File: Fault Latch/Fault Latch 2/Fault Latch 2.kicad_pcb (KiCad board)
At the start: 2 copper layers, 110 x 90 mm, 108 parts, among them K101 Fujitsu_FTR-LYAA005x, K102 Fujitsu_FTR-LYAA005x, K103 Fujitsu_FTR-LYAA005x, Q101 Q_NPN_BEC, Q102 Q_NPN_BEC, Q103 Q_NPN_BEC, Q104 Q_NPN_BEC, Q105 Q_NMOS_GSD, Q106 Q_NMOS_GSD, Q107 Q_PMOS_GSD, Q108 Q_PMOS_GSD, Q109 Q_NMOS_GDS, Q110 Q_NPN_BEC, Q111 Q_NPN_BEC, Q112 Q_NMOS_GSD, Q113 Q_PMOS_GSD, SW101 SW_Omron_B3FS, SW102 SW_Omron_B3FS, SW103 SW_Omron_B3FS, U101 SFH617A-1, U102 SFH617A-1, U103 SFH617A-1, U104 74AHC1G00, U105 74AHC1G00, U106 74AHC1G00, U107 74LS279, U108 641964-1, U109 SFH617A-1, U110 SFH617A-1, U111 641964-1, U112 641964-1, U113 641964-1, U114 641964-1, U115 641964-1, U116 641964-1, U117 74AHC1G00, U118 LM555xM, U119 74AHC1G00, U120 641964-1, U121 SFH617A-1, U122 641964-1

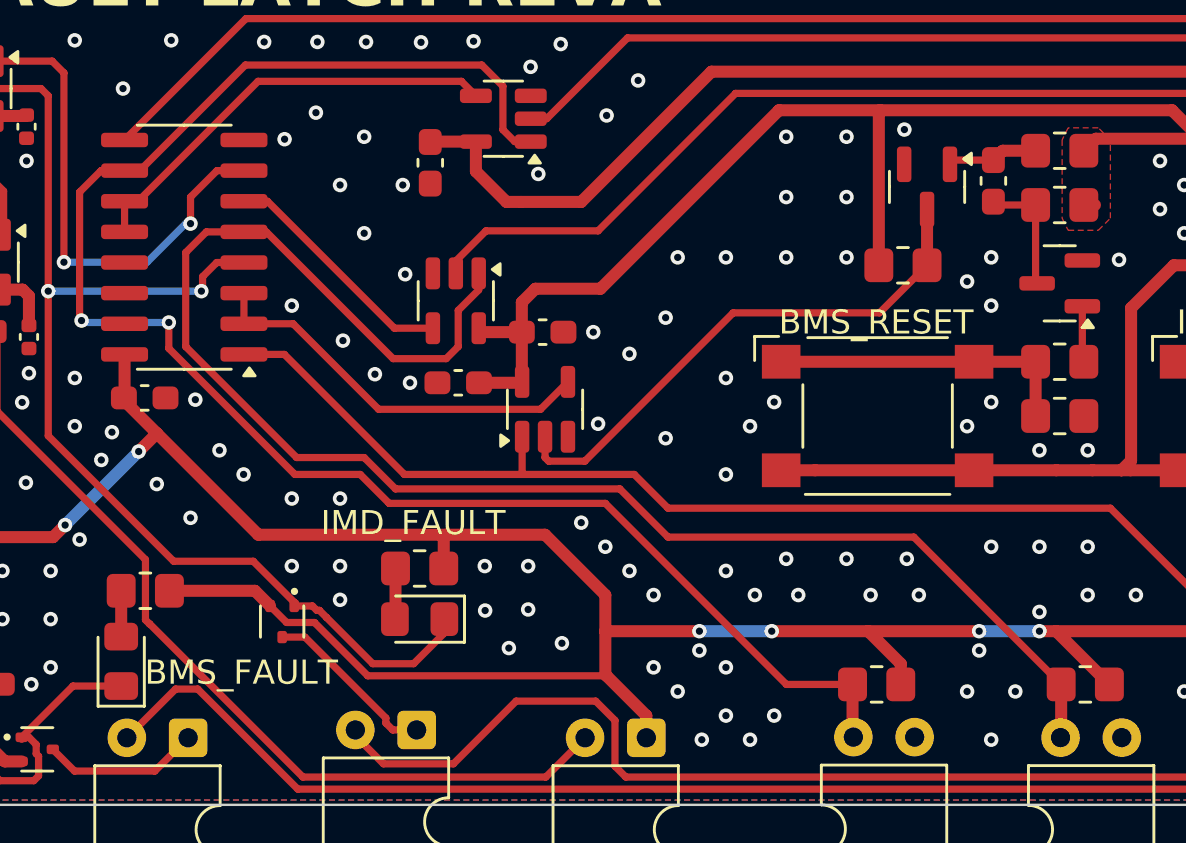
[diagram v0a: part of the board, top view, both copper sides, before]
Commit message: Fixed errors on schematic. Need to update pcb layout
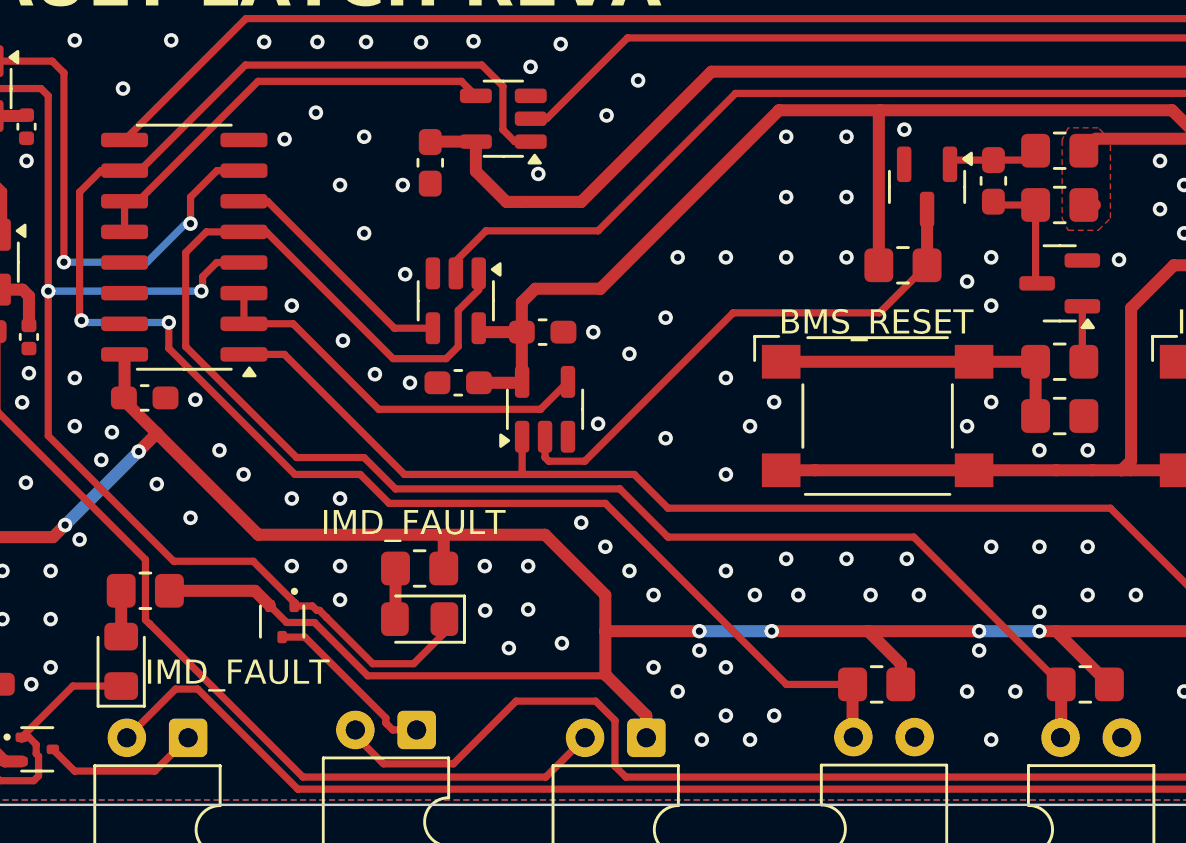
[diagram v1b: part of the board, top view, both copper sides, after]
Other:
- board text removed: "BMS_FAULT"
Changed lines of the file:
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@@
 		(pcbplotparams
 			(layerselection 0x00000000_00000000_55555555_5755f5ff)
-			(plot_on_all_layers_selection 0x00000000_00000000_00000000_00000000)
+			(plot_on_all_layers_selection 0x00000000_00000000_00000000_2200a0af)
 			(disableapertmacros no)
 			(usegerberextensions yes)
@@
 			(crossoutdnponfab yes)
 			(subtractmaskfromsilk yes)
-			(outputformat 1)
+			(outputformat 4)
 			(mirror no)
 			(drillshape 0)
 			(scaleselection 1)
-			(outputdirectory "Gerber/")
+			(outputdirectory "PDF/")
 		)
 	)
@@
 		)
 	)
-	(gr_text "BMS_FAULT"
+	(gr_text "IMD_FAULT"
 		(at 90.122 76.872 0)
 		(layer "F.SilkS" knockout)
@@
 	)
 	(segment
-		(start 127.0625 54.65)
-		(end 125.7 54.65)
-		(width 0.5)
+		(start 123.6875 55.0375)
+		(end 123.5125 55.2125)
+		(width 0.3)
 		(layer "F.Cu")
 		(net 4)
 	)
 	(segment
-		(start 125.7 54.65)
-		(end 125.3125 55.0375)
-		(width 0.5)
+		(start 126.675 55.0375)
+		(end 127.0625 54.65)
+		(width 0.3)
 		(layer "F.Cu")
 		(net 4)
 	)
 	(segment
-		(start 123.6875 55.0375)
-		(end 123.5125 55.2125)
+		(start 125.3125 55.0375)
+		(end 123.6875 55.0375)
 		(width 0.3)
 		(layer "F.Cu")
@@
 	(segment
 		(start 125.3125 55.0375)
-		(end 123.6875 55.0375)
+		(end 126.675 55.0375)
 		(width 0.3)
 		(layer "F.Cu")
